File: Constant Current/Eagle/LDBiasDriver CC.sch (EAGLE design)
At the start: 24 parts, among them IC1 MCP1703-5002E/DB, IC2 MLD203P1, IC3 LM358D

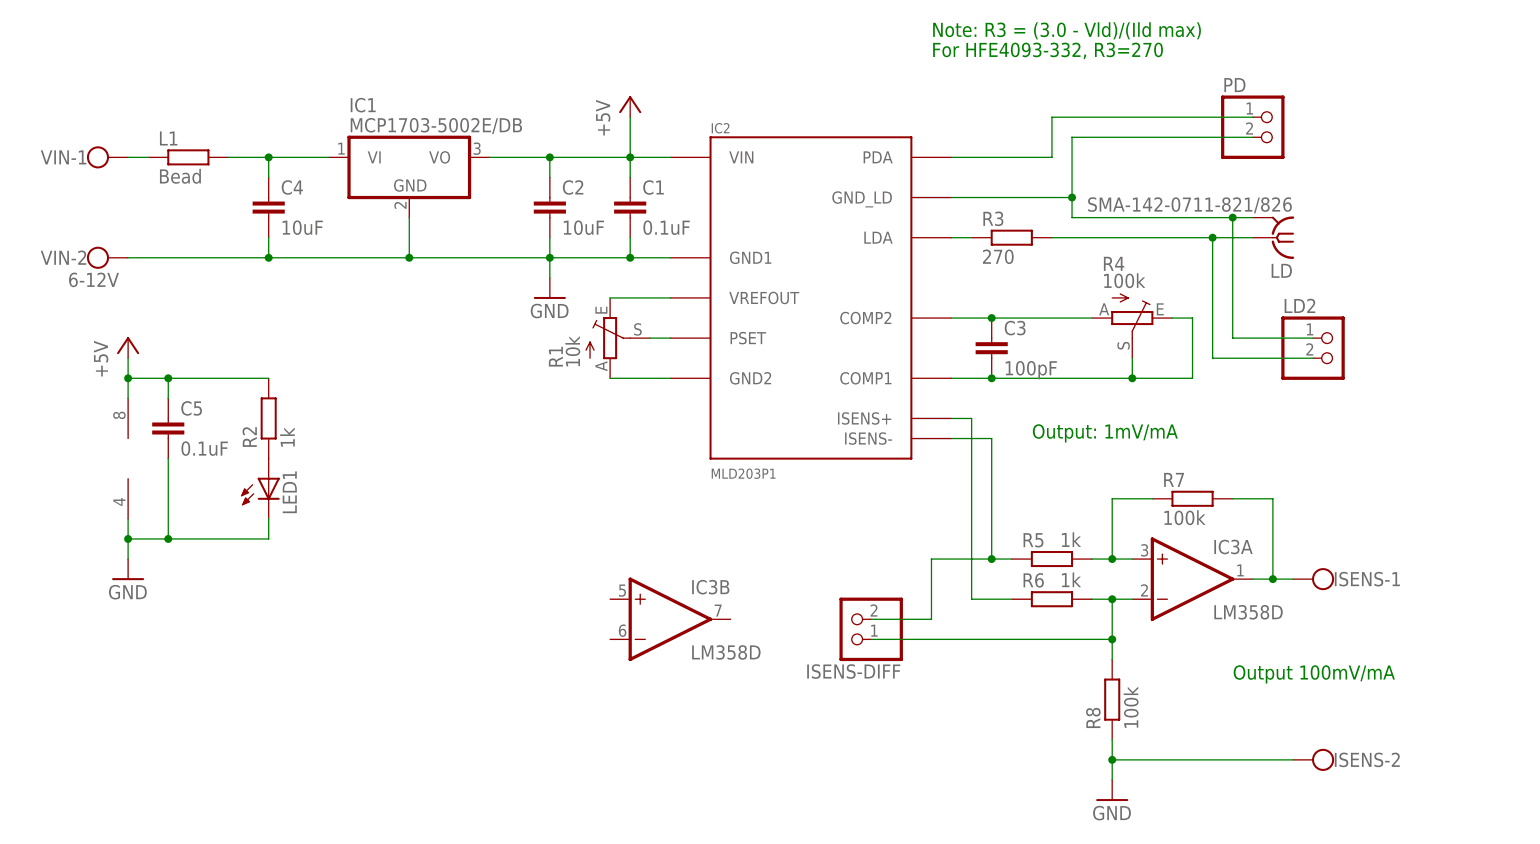
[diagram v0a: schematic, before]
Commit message: Added a CC version
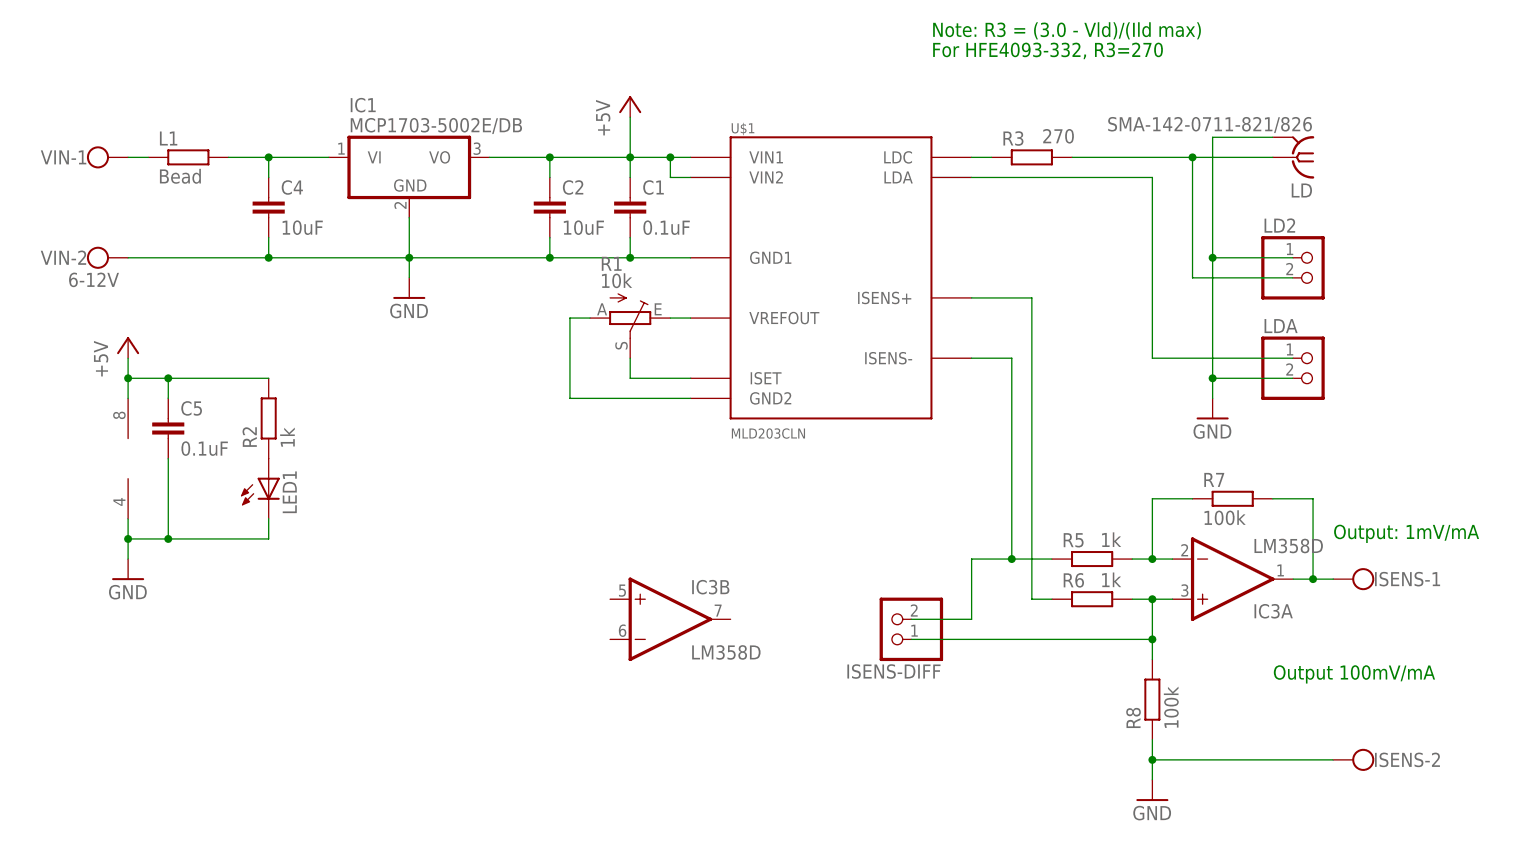
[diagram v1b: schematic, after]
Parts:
- removed C3: 100pF, rcl:C-EUC0805
- removed IC2: MLD203P1, laser diode:MLD203P1
- removed PD: (no value), pinhead:PINHD-1X2
- removed R4: 100k, pot:TRIM_EU-RJ9W
- added LDA: (no value), pinhead:PINHD-1X2
- added U$1: MLD203CLN, laser diode:MLD203CLN
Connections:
- removed net N$10: IC2.GND_LD, LD.2, LD2.1, PD.2
- removed net N$12: C3.2, IC2.COMP1, R4.E, R4.S
- removed net N$13: C3.1, IC2.COMP2, R4.A
- net +5V: now also U$1.VIN1, U$1.VIN2; no longer IC2.VIN
- net GND: now also LD.2, LD2.1, LDA.2, U$1.GND1; no longer IC2.GND1
- net N$11: now also LDA.1, U$1.LDA; no longer IC2.PDA, PD.1
- net N$16: now also IC3A.-IN; no longer IC3A.+IN
- net N$17: now also IC3A.+IN; no longer IC3A.-IN
- net N$2: now also R1.E, U$1.VREFOUT; no longer IC2.PSET, R1.S
- net N$4: now also R1.S, U$1.ISET; no longer IC2.VREFOUT, R1.E
- net N$5: now also U$1.GND2; no longer IC2.GND2
- net N$6: now also U$1.ISENS+; no longer IC2.ISENS+
- net N$7: now also U$1.ISENS-; no longer IC2.ISENS-
- net N$9: now also U$1.LDC; no longer IC2.LDA
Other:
- moved on the sheet: IC3A, ISENS-1, ISENS-2, ISENS-DIFF, LD, LD2, R1, R3, R5, R6, R7, R8
